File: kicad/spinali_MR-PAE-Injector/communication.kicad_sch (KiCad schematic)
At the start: 17 parts, among them J3 CAN0A, J4 CAN0B, U12 TJA1462ATK

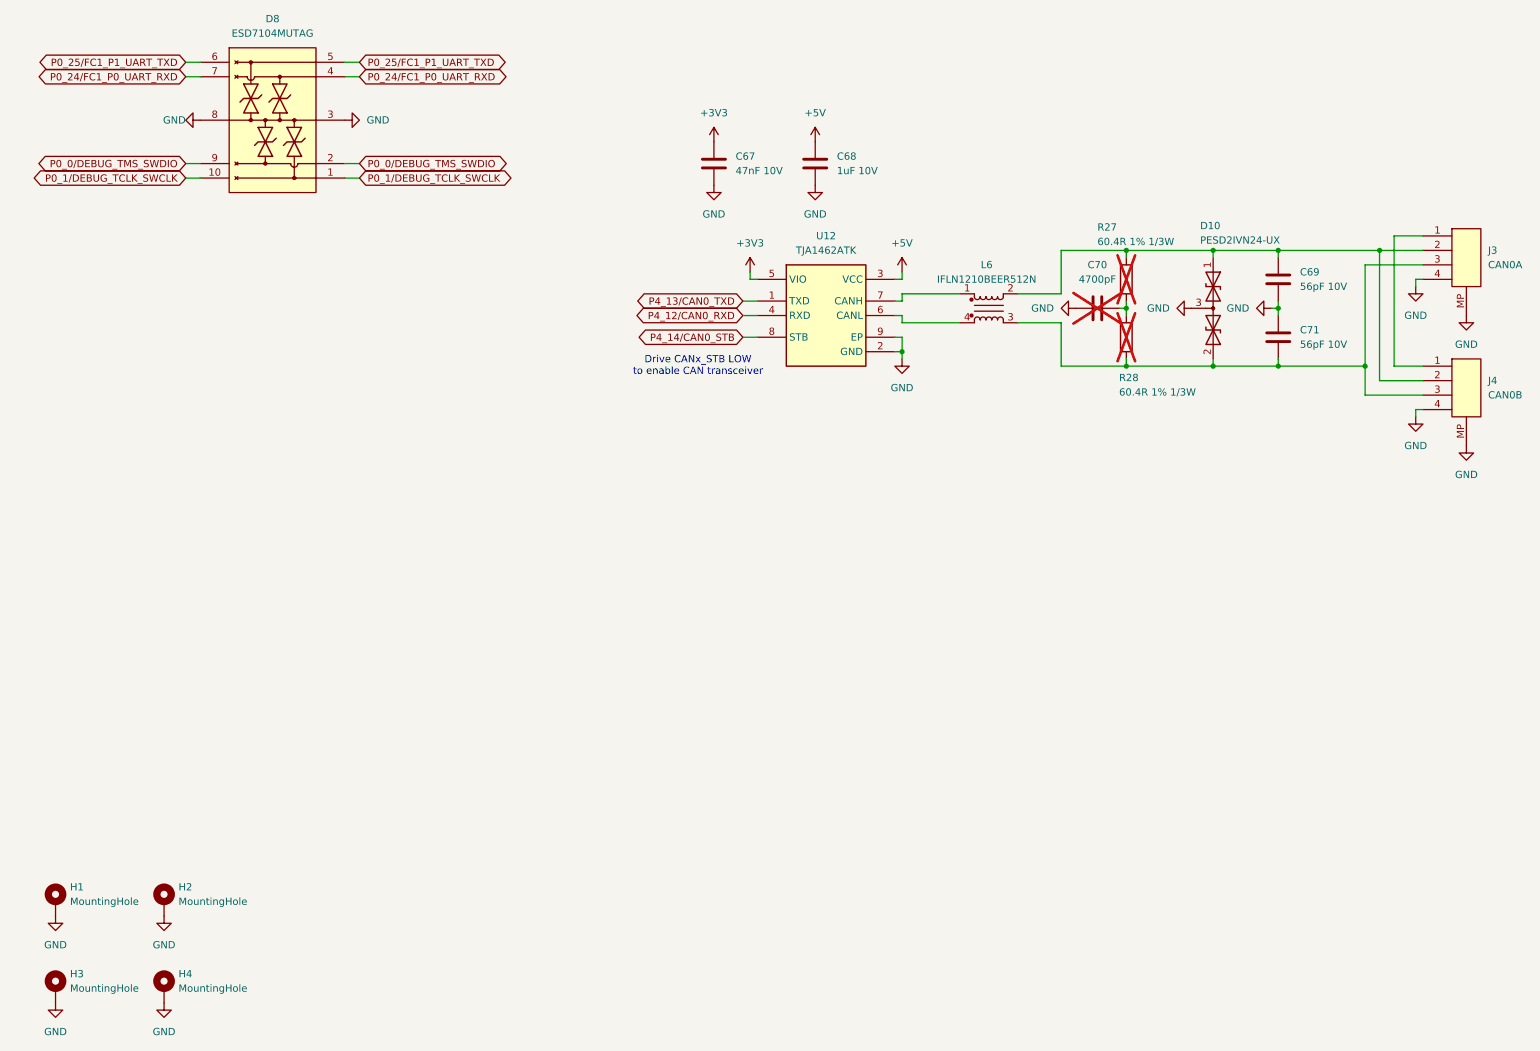
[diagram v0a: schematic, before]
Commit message: Draft design work
Cutting original schematics to basics.
Questions aroung the LM5160 regulator
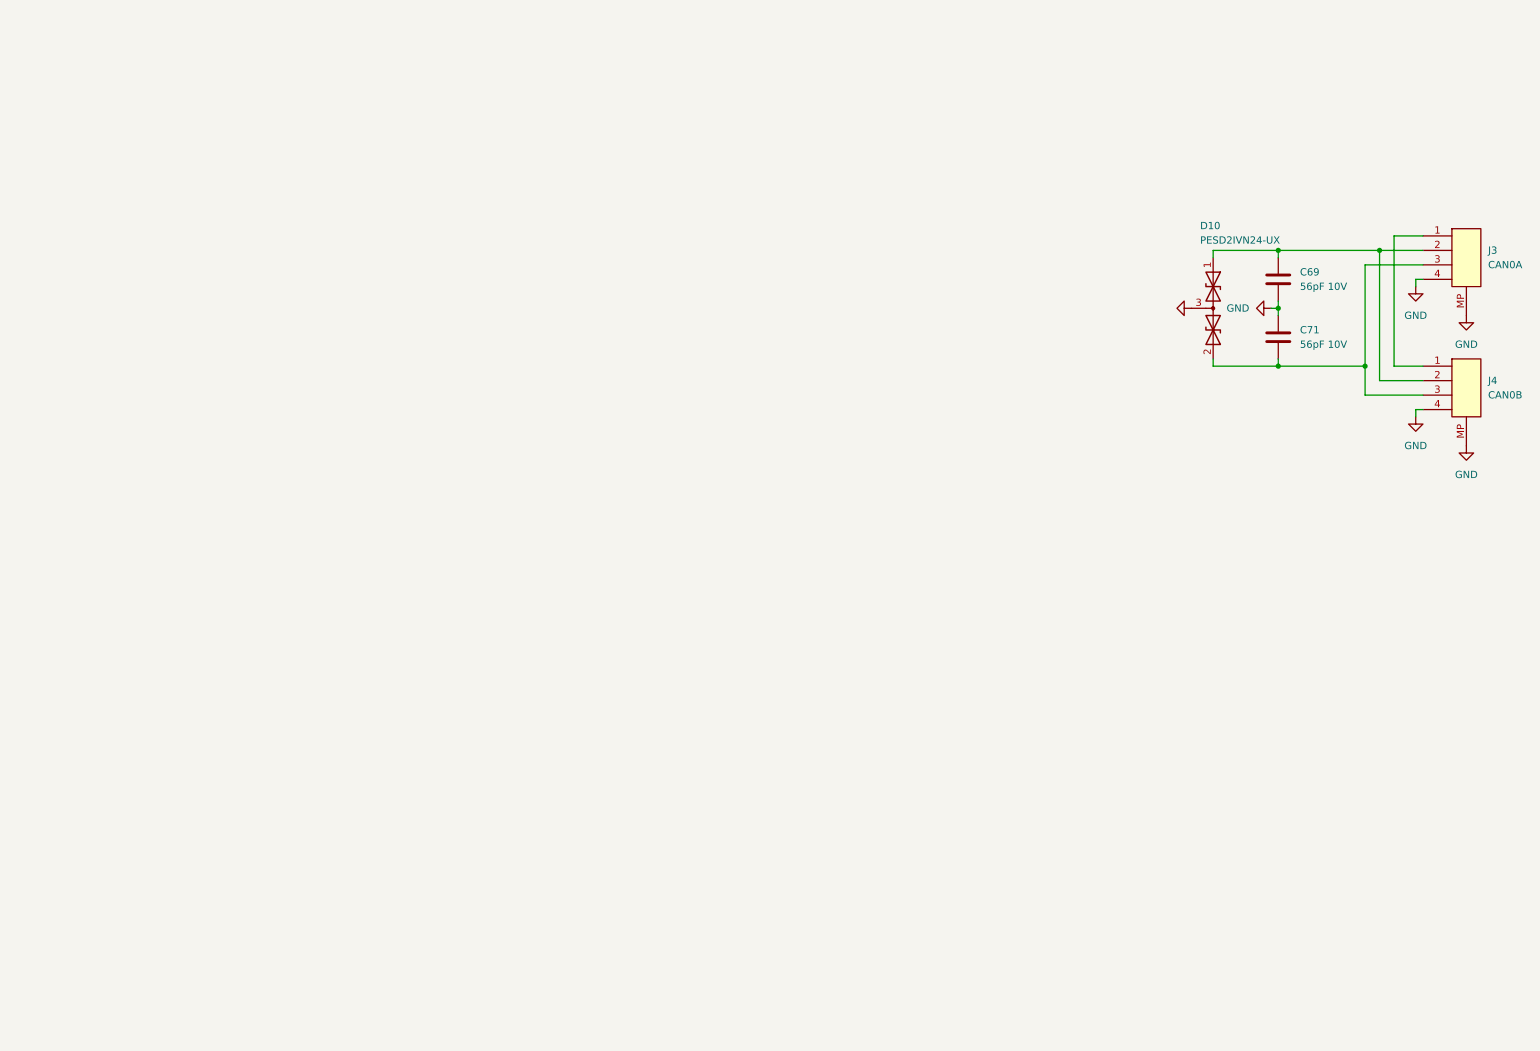
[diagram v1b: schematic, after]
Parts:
- removed C67: 47nF 10V, Capacitor_SMD:C_0402_1005Metric, symbol Device:C
- removed C68: 1uF 10V, Capacitor_SMD:C_0402_1005Metric, symbol Device:C
- removed C70: 4700pF, Capacitor_SMD:C_0402_1005Metric, symbol Device:C
- removed D8: ESD7104MUTAG, TVS:ESD8104MUTAG, symbol TVS:ESD7104MUTAG
- removed H1, H2, H3, H4: MountingHole, MountingHole:MountingHole_3.2mm_M3_DIN965_Pad, symbol Mechanical:MountingHole_Pad
- removed L6: IFLN1210BEER512N, Inductors:IFLN1210BEER512N, symbol Inductors:IFLN1210BEER512N
- removed R27, R28: 60.4R 1% 1/3W, Resistor_SMD:R_0603_1608Metric, symbol Resistors:CRCW060360R4FKEAHP
- removed U12: TJA1462ATK, NXP_HV:SON65P300X300X100-9N-D, symbol Transceivers:TJA1462ATK
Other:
- note removed: "Drive CANx_STB LOW to enable CAN transceiver"

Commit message: ongoing edits and prep
added symbols for 2 pin  and 3 pin headers.
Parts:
- removed C69, C71: 56pF 10V, Capacitor_SMD:C_0402_1005Metric, symbol Device:C
- removed D10: PESD2IVN24-UX, Package_TO_SOT_SMD:SOT-323_SC-70, symbol Diodes:PESD2IVN24-UX
- removed J3: CAN0A, Connector_JST:JST_GH_SM04B-GHS-TB_1x04-1MP_P1.25mm_Horizontal, symbol Connectors:JST_GH_SM04B-GHS-TB
- removed J4: CAN0B, Connector_JST:JST_GH_SM04B-GHS-TB_1x04-1MP_P1.25mm_Horizontal, symbol Connectors:JST_GH_SM04B-GHS-TB
